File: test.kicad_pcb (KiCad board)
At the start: 2 copper layers, 1 part, among them IC1 ESP32-S3-WROOM-1-N16

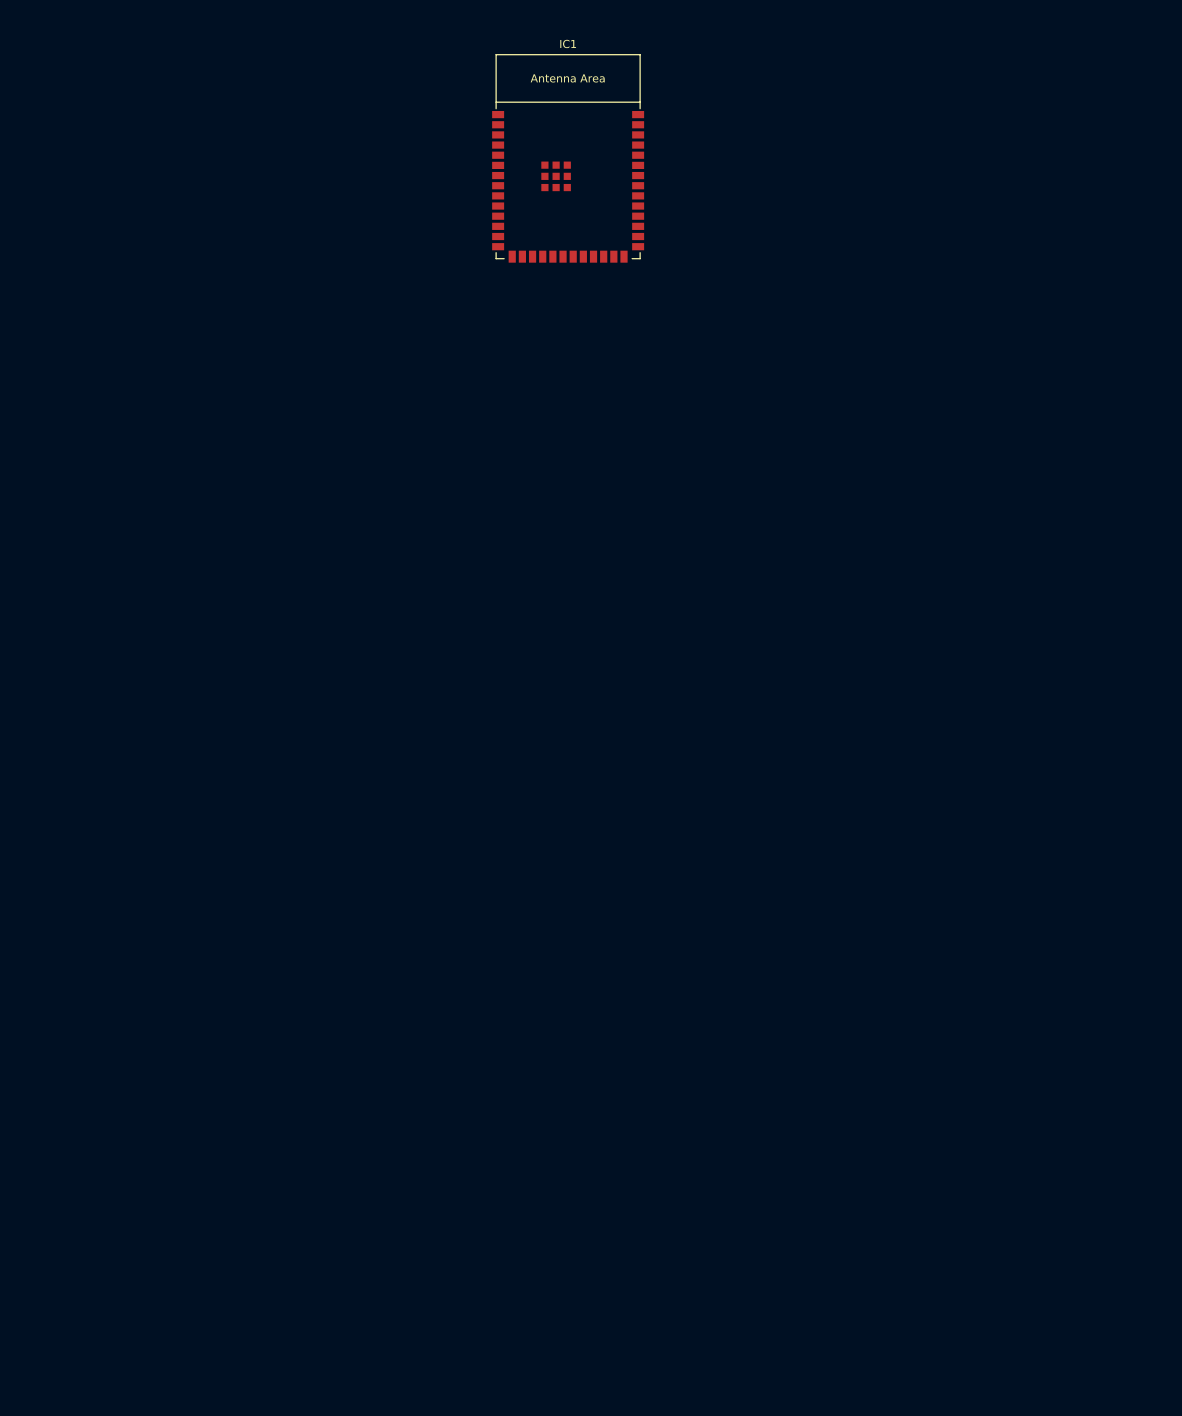
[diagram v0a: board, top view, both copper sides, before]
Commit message: esp32 and power
added first try of battery, connecotrs and esp32.
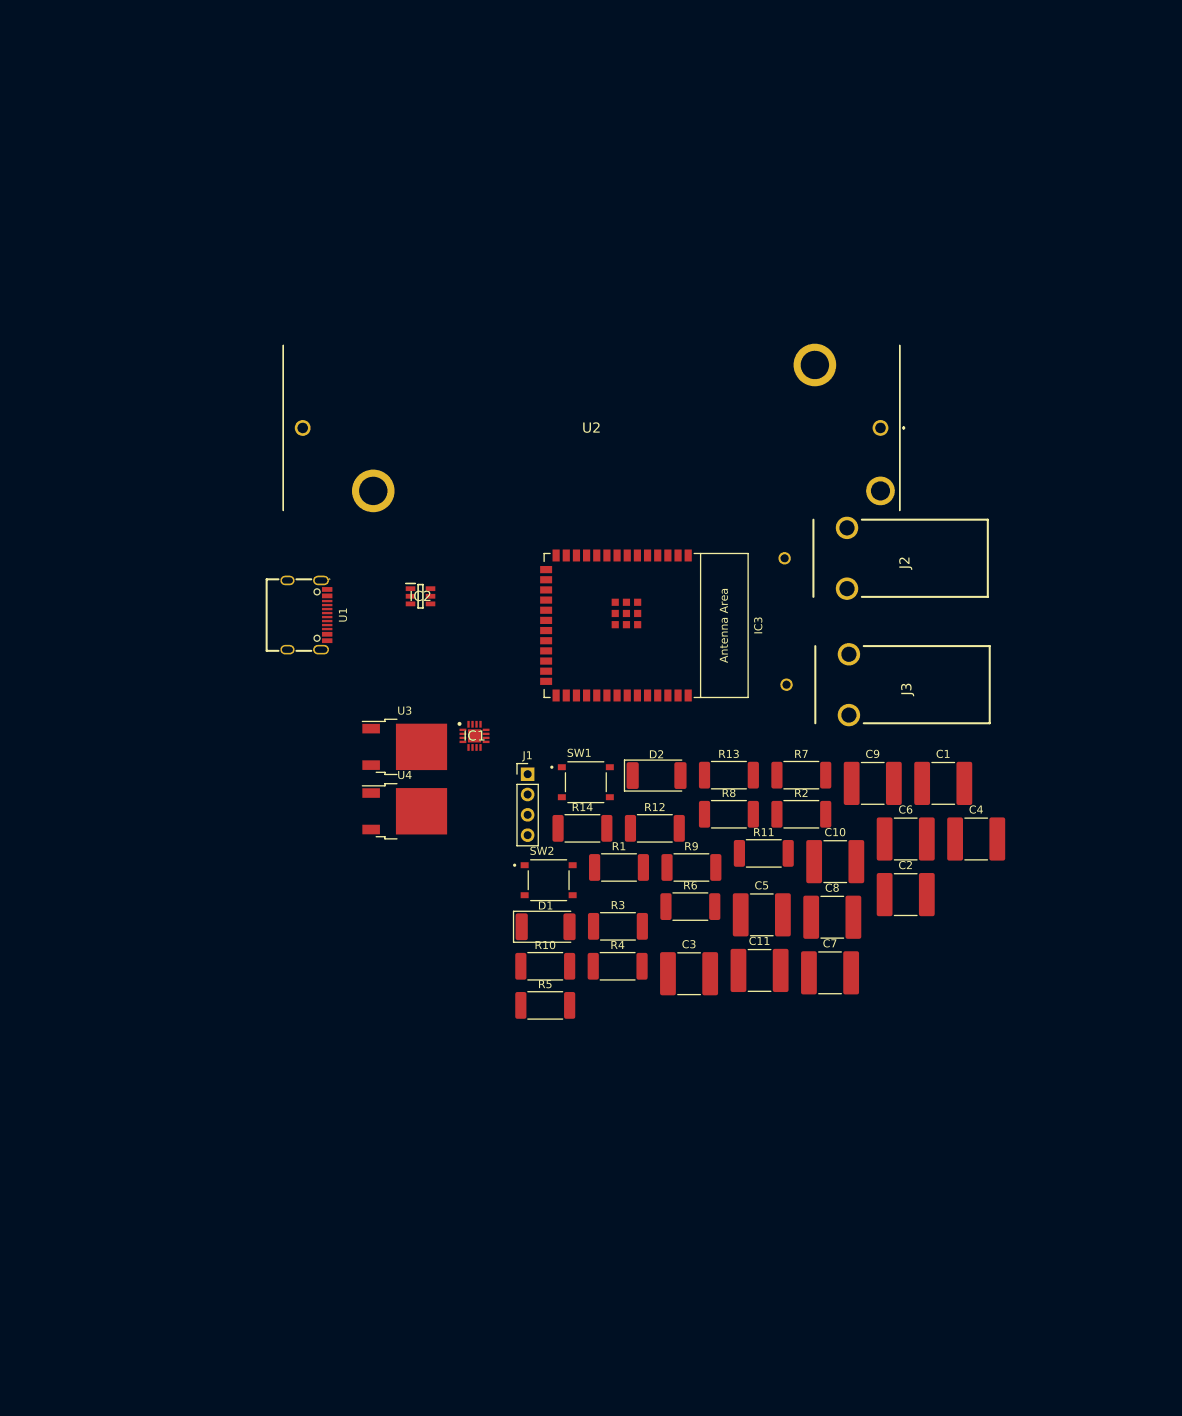
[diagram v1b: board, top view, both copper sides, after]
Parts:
- added C1: 1u, Capacitor_SMD:C_2220_5650Metric_Pad1.97x5.40mm_HandSolder, F.Cu at (119.2, 131.2)
- added C10: 10u, Capacitor_SMD:C_2220_5650Metric_Pad1.97x5.40mm_HandSolder, F.Cu at (105.7, 141.0)
- added C11: 100n, Capacitor_SMD:C_2220_5650Metric_Pad1.97x5.40mm_HandSolder, F.Cu at (96.2, 154.6)
- added C2: 4u7, Capacitor_SMD:C_2220_5650Metric_Pad1.97x5.40mm_HandSolder, F.Cu at (114.5, 145.1)
- added C3: 100n, Capacitor_SMD:C_2220_5650Metric_Pad1.97x5.40mm_HandSolder, F.Cu at (87.4, 155.0)
- added C4: 4u7, Capacitor_SMD:C_2220_5650Metric_Pad1.97x5.40mm_HandSolder, F.Cu at (123.3, 138.2)
- added C5: 22u, Capacitor_SMD:C_2220_5650Metric_Pad1.97x5.40mm_HandSolder, F.Cu at (96.5, 147.7)
- added C6: 10u, Capacitor_SMD:C_2220_5650Metric_Pad1.97x5.40mm_HandSolder, F.Cu at (114.5, 138.2)
- added C7: 10u, Capacitor_SMD:C_2220_5650Metric_Pad1.97x5.40mm_HandSolder, F.Cu at (105.0, 154.9)
- added C8: 0.1u, Capacitor_SMD:C_2220_5650Metric_Pad1.97x5.40mm_HandSolder, F.Cu at (105.3, 148.0)
- added C9: 10u, Capacitor_SMD:C_2220_5650Metric_Pad1.97x5.40mm_HandSolder, F.Cu at (110.4, 131.2)
- added D1: LED_PowerOn, LED_SMD:LED_2512_6332Metric_Pad1.52x3.35mm_HandSolder, F.Cu at (69.5, 149.2)
- added D2: LED_Charging, LED_SMD:LED_2512_6332Metric_Pad1.52x3.35mm_HandSolder, F.Cu at (83.4, 130.3)
- added IC1: BQ24074RGTR, project_library:BQ24074RGTR, F.Cu at (60.6, 125.3)
- added IC2: USBLC6-2SC6, project_library:USBLC6-2SC6, F.Cu at (53.9, 107.8)
- added J1: UART0, Connector_PinHeader_2.54mm:PinHeader_1x04_P2.54mm_Vertical, F.Cu at (67.2, 130.1)
- added J2: 73100-0105, project_library:73100-0105, F.Cu at (124.8, 103.1)
- added J3: 73100-0105, project_library:73100-0105, F.Cu at (125.0, 118.9)
- added R1: 1M, Resistor_SMD:R_2512_6332Metric_Pad1.40x3.35mm_HandSolder, F.Cu at (78.7, 141.8)
- added R10: 39, Resistor_SMD:R_2512_6332Metric_Pad1.40x3.35mm_HandSolder, F.Cu at (69.4, 154.1)
- added R11: 120, Resistor_SMD:R_2512_6332Metric_Pad1.40x3.35mm_HandSolder, F.Cu at (96.8, 140.0)
- added R12: 470, Resistor_SMD:R_2512_6332Metric_Pad1.40x3.35mm_HandSolder, F.Cu at (83.1, 136.9)
- added R13: 470, Resistor_SMD:R_2512_6332Metric_Pad1.40x3.35mm_HandSolder, F.Cu at (92.4, 130.2)
- added R14: 5k1, Resistor_SMD:R_2512_6332Metric_Pad1.40x3.35mm_HandSolder, F.Cu at (74.1, 136.9)
- added R2: 5k1, Resistor_SMD:R_2512_6332Metric_Pad1.40x3.35mm_HandSolder, F.Cu at (101.5, 135.1)
- added R3: 4k12, Resistor_SMD:R_2512_6332Metric_Pad1.40x3.35mm_HandSolder, F.Cu at (78.5, 149.1)
- added R4: 5k1, Resistor_SMD:R_2512_6332Metric_Pad1.40x3.35mm_HandSolder, F.Cu at (78.5, 154.1)
- added R5: 1k5, Resistor_SMD:R_2512_6332Metric_Pad1.40x3.35mm_HandSolder, F.Cu at (69.4, 159.0)
- added R6: 4k12, Resistor_SMD:R_2512_6332Metric_Pad1.40x3.35mm_HandSolder, F.Cu at (87.6, 146.6)
- added R7: 1k5, Resistor_SMD:R_2512_6332Metric_Pad1.40x3.35mm_HandSolder, F.Cu at (101.5, 130.2)
- added R8: 4k12, Resistor_SMD:R_2512_6332Metric_Pad1.40x3.35mm_HandSolder, F.Cu at (92.4, 135.1)
- added R9: 5k1, Resistor_SMD:R_2512_6332Metric_Pad1.40x3.35mm_HandSolder, F.Cu at (87.7, 141.8)
- added SW1: Reset, project_library:SW_TS-1187A-B-A-B, F.Cu at (74.5, 131.1)
- added SW2: Boot, project_library:SW_TS-1187A-B-A-B, F.Cu at (69.9, 143.3)
- added U1: USB-TYPE-C-018, project_library:USB-TYPE-C-018, F.Cu at (38.4, 110.2)
- added U2: 1043, project_library:1043, F.Cu at (111.3, 86.8)
- added U3: LD1086DT33TR, Package_TO_SOT_SMD:TO-252-2, F.Cu at (51.9, 126.7)
- added U4: LD1086DT33TR, Package_TO_SOT_SMD:TO-252-2, F.Cu at (51.9, 134.7)
- moved IC3 56.0 mm to (79.0, 111.5), turned to -90 degrees
- renumbered IC1 to IC3
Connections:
- IC3 pad 1: unconnected-(IC1-Pad1) -> GND
- IC3 pad 13: unconnected-(IC1-Pad13) -> /USB_D-
- IC3 pad 14: unconnected-(IC1-Pad14) -> /USB_D+
- IC3 pad 2: unconnected-(IC1-Pad2) -> +3V3
- IC3 pad 27: unconnected-(IC1-Pad27) -> Net-(C11-Pad1)
- IC3 pad 3: unconnected-(IC1-Pad3) -> Net-(C3-Pad1)
- IC3 pad 36: unconnected-(IC1-Pad36) -> /RX0
- IC3 pad 37: unconnected-(IC1-Pad37) -> /TX0
- IC3 pad 40: unconnected-(IC1-Pad40) -> GND
- IC3 pad 41: unconnected-(IC1-Pad41) -> GND

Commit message: first try of front end
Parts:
- removed the R3 at (78.5, 149.1)
- added C12: 10u, Capacitor_SMD:C_1206_3216Metric_Pad1.33x1.80mm_HandSolder, F.Cu at (110.9, 116.5)
- added K1: AQY210EHA, project_library:AQY210EHAX, F.Cu at (74.1, 125.4)
- added U2: 1043, project_library:1043, B.Cu at (56.9, 101.0)
- C1, C10, C11, C2, C3, C4, C5, C6, C7, C8, C9: footprint Capacitor_SMD:C_2220_5650Metric_Pad1.97x5.40mm_HandSolder -> Capacitor_SMD:C_1206_3216Metric_Pad1.33x1.80mm_HandSolder
- D1: value LED_PowerOn -> LED_PowerOn?
- IC1: value BQ24074RGTR -> QFN50P300X300X100-17N-D
- IC2: value USBLC6-2SC6 -> SOT95P280X145-6N
- J1, J2, J3: moved to B.Cu
- R1, R2, R4, R7: footprint Resistor_SMD:R_2512_6332Metric_Pad1.40x3.35mm_HandSolder -> Resistor_SMD:R_1206_3216Metric_Pad1.30x1.75mm_HandSolder
- R10: renamed from R11; footprint Resistor_SMD:R_2512_6332Metric_Pad1.40x3.35mm_HandSolder -> Resistor_SMD:R_1206_3216Metric_Pad1.30x1.75mm_HandSolder
- R11: renamed from R12; footprint Resistor_SMD:R_2512_6332Metric_Pad1.40x3.35mm_HandSolder -> Resistor_SMD:R_1206_3216Metric_Pad1.30x1.75mm_HandSolder
- R12: renamed from R13; footprint Resistor_SMD:R_2512_6332Metric_Pad1.40x3.35mm_HandSolder -> Resistor_SMD:R_1206_3216Metric_Pad1.30x1.75mm_HandSolder
- R13: renamed from R14; footprint Resistor_SMD:R_2512_6332Metric_Pad1.40x3.35mm_HandSolder -> Resistor_SMD:R_1206_3216Metric_Pad1.30x1.75mm_HandSolder
- R3: renamed from R6; value 4k12 -> 1k; footprint Resistor_SMD:R_2512_6332Metric_Pad1.40x3.35mm_HandSolder -> Resistor_SMD:R_1206_3216Metric_Pad1.30x1.75mm_HandSolder
- R5: renamed from R8; value 4k12 -> 820; footprint Resistor_SMD:R_2512_6332Metric_Pad1.40x3.35mm_HandSolder -> Resistor_SMD:R_1206_3216Metric_Pad1.30x1.75mm_HandSolder
- R6: renamed from R5; footprint Resistor_SMD:R_2512_6332Metric_Pad1.40x3.35mm_HandSolder -> Resistor_SMD:R_1206_3216Metric_Pad1.30x1.75mm_HandSolder
- R8: renamed from R9; footprint Resistor_SMD:R_2512_6332Metric_Pad1.40x3.35mm_HandSolder -> Resistor_SMD:R_1206_3216Metric_Pad1.30x1.75mm_HandSolder
- R9: renamed from R10; footprint Resistor_SMD:R_2512_6332Metric_Pad1.40x3.35mm_HandSolder -> Resistor_SMD:R_1206_3216Metric_Pad1.30x1.75mm_HandSolder
- U1: value USB-TYPE-C-018 -> USB-C_SMD-TYPE-C-31-M-12; moved to B.Cu
- U3: renamed from U2; moved to B.Cu
- moved J1 69.3 mm to (135.0, 115.5)
- moved C3 68.0 mm to (122.0, 96.4)
- moved U3 64.8 mm to (56.9, 122.0), turned to 180 degrees
- moved R4 63.8 mm to (105.5, 96.3)
- moved R6 62.8 mm to (95.0, 101.6)
- moved SW2 57.4 mm to (40.5, 94.0)
- moved C11 56.7 mm to (126.8, 106.9)
- moved D1 55.8 mm to (40.5, 101.5), turned to -90 degrees
- moved C7 55.7 mm to (121.9, 101.8)
- moved R3 51.9 mm to (100.2, 96.3)
- moved R9 51.5 mm to (90.0, 106.9)
- moved C8 51.2 mm to (127.3, 101.8)
- moved C2 48.8 mm to (116.6, 96.4)
- moved C5 48.1 mm to (110.9, 101.8)
- moved R13 47.4 mm to (110.8, 106.8)
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- renumbered U3 to U4, U4 to U5
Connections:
- IC1 pad 15: Net-(IC1-Pad15) -> GND
- IC2 pad 4: /USB_D+ -> Net-(IC2-Pad4)
- IC2 pad 6: /USB_D- -> Net-(IC2-Pad6)
- IC3 pad 20: unconnected-(IC3-Pad20) -> /MISO
- IC3 pad 21: unconnected-(IC3-Pad21) -> /MOSI
- IC3 pad 22: unconnected-(IC3-Pad22) -> /SCLK
- IC3 pad 8: unconnected-(IC3-Pad8) -> /CS
- U1 pad A6: /USB_D+ -> Net-(IC2-Pad4)
- U1 pad A7: /USB_D- -> Net-(IC2-Pad6)
- U1 pad B6: /USB_D+ -> Net-(IC2-Pad4)
- U1 pad B7: /USB_D- -> Net-(IC2-Pad6)
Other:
- board outline added: 112 x 43 mm
